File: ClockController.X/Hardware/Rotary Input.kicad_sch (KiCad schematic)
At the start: 7 parts

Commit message: Updated most footprints
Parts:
- C7, C8, C9: footprint Clock Controller:CAP_0603 -> Capacitor_SMD:C_0603_1608Metric
- R12, R13, R8: footprint Clock Controller:RES_0603 -> Resistor_SMD:R_0603_1608Metric
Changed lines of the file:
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@@
 			)
 		)
-		(property "Footprint" "Clock Controller:CAP_0603"
+		(property "Footprint" "Capacitor_SMD:C_0603_1608Metric"
 			(at 111.76 82.55 0)
 			(effects
@@
 			)
 		)
-		(property "Footprint" "Clock Controller:CAP_0603"
+		(property "Footprint" "Capacitor_SMD:C_0603_1608Metric"
 			(at 111.76 132.08 0)
 			(effects
@@
 			)
 		)
-		(property "Footprint" "Clock Controller:RES_0603"
+		(property "Footprint" "Resistor_SMD:R_0603_1608Metric"
 			(at 123.19 82.55 0)
 			(effects
@@
 			)
 		)
-		(property "Footprint" "Clock Controller:CAP_0603"
+		(property "Footprint" "Capacitor_SMD:C_0603_1608Metric"
 			(at 182.88 132.08 0)
 			(effects
@@
 			)
 		)
-		(property "Footprint" "Clock Controller:RES_0603"
+		(property "Footprint" "Resistor_SMD:R_0603_1608Metric"
 			(at 123.19 113.03 0)
 			(effects
@@
 			)
 		)
-		(property "Footprint" "Clock Controller:RES_0603"
+		(property "Footprint" "Resistor_SMD:R_0603_1608Metric"
 			(at 173.99 113.03 0)
 			(effects

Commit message: Replacing many thin traces with poured zones.
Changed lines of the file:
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@@
 (kicad_sch
-	(version 20231120)
+	(version 20250114)
 	(generator "eeschema")
-	(generator_version "8.0")
+	(generator_version "9.0")
 	(paper "A4")
+	(text "10k"
+		(exclude_from_sim no)
+		(at 124.46 114.595 90)
+		(effects
+			(font
+				(size 1.48 1.48)
+			)
+			(justify left top)
+		)
+	)
+	(text "C7"
+		(exclude_from_sim no)
+		(at 109.849 133.372 90)
+		(effects
+			(font
+				(size 1.48 1.48)
+			)
+			(justify left bottom)
+		)
+	)
+	(text "10k"
+		(exclude_from_sim no)
+		(at 124.46 84.115 90)
+		(effects
+			(font
+				(size 1.48 1.48)
+			)
+			(justify left top)
+		)
+	)
+	(text "C8"
+		(exclude_from_sim no)
+		(at 109.849 83.842 90)
+		(effects
+			(font
+				(size 1.48 1.48)
+			)
+			(justify left bottom)
+		)
+	)
+	(text "10nF"
+		(exclude_from_sim no)
+		(at 184.791 134.354 90)
+		(effects
+			(font
+				(size 1.48 1.48)
+			)
+			(justify left top)
+		)
+	)
+	(text "10k"
+		(exclude_from_sim no)
+		(at 175.26 114.595 90)
+		(effects
+			(font
+				(size 1.48 1.48)
+			)
+			(justify left top)
+		)
+	)
+	(text "R12"
+		(exclude_from_sim no)
+		(at 121.92 114.704 90)
+		(effects
+			(font
+				(size 1.48 1.48)
+			)
+			(justify left bottom)
+		)
+	)
+	(text "C9"
+		(exclude_from_sim no)
+		(at 180.969 133.336 90)
+		(effects
+			(font
+				(size 1.48 1.48)
+			)
+			(justify left bottom)
+		)
+	)
+	(text "10nF"
+		(exclude_from_sim no)
+		(at 113.671 84.824 90)
+		(effects
+			(font
+				(size 1.48 1.48)
+			)
+			(justify left top)
+		)
+	)
+	(text "RC5"
+		(exclude_from_sim no)
+		(at 125.222 61.722 0)
+		(effects
+			(font
+				(size 1.48 1.48)
+			)
+			(justify right bottom)
+		)
+	)
+	(text "RC3"
+		(exclude_from_sim no)
+		(at 171.958 136.144 0)
+		(effects
+			(font
+				(size 1.48 1.48)
+			)
+			(justify left bottom)
+		)
+	)
+	(text "R13"
+		(exclude_from_sim no)
+		(at 172.72 114.704 90)
+		(effects
+			(font
+				(size 1.48 1.48)
+			)
+			(justify left bottom)
+		)
+	)
+	(text "10nF"
+		(exclude_from_sim no)
+		(at 113.671 134.354 90)
+		(effects
+			(font
+				(size 1.48 1.48)
+			)
+			(justify left top)
+		)
+	)
+	(text "RC4"
+		(exclude_from_sim no)
+		(at 125.476 136.144 0)
+		(effects
+			(font
+				(size 1.48 1.48)
+			)
+			(justify right bottom)
+		)
+	)
+	(text "S1"
+		(exclude_from_sim no)
+		(at 127.341 87.63 0)
+		(effects
+			(font
+				(size 1.48 1.48)
+			)
+			(justify left bottom)
+		)
+	)
+	(text "R8"
+		(exclude_from_sim no)
+		(at 121.92 83.805 90)
+		(effects
+			(font
+				(size 1.48 1.48)
+			)
+			(justify left bottom)
+		)
+	)
 	(junction
 		(at 123.19 72.39)
@@
 		)
 	)
-	(text "10k"
-		(exclude_from_sim no)
-		(at 124.46 114.595 90)
-		(effects
-			(font
-				(size 1.48 1.48)
-			)
-			(justify left top)
-		)
-	)
-	(text "C7"
-		(exclude_from_sim no)
-		(at 109.849 133.372 90)
-		(effects
-			(font
-				(size 1.48 1.48)
-			)
-			(justify left bottom)
-		)
-	)
-	(text "10k"
-		(exclude_from_sim no)
-		(at 124.46 84.115 90)
-		(effects
-			(font
-				(size 1.48 1.48)
-			)
-			(justify left top)
-		)
-	)
-	(text "C8"
-		(exclude_from_sim no)
-		(at 109.849 83.842 90)
-		(effects
-			(font
-				(size 1.48 1.48)
-			)
-			(justify left bottom)
-		)
-	)
-	(text "10nF"
-		(exclude_from_sim no)
-		(at 184.791 134.354 90)
-		(effects
-			(font
-				(size 1.48 1.48)
-			)
-			(justify left top)
-		)
-	)
-	(text "10k"
-		(exclude_from_sim no)
-		(at 175.26 114.595 90)
-		(effects
-			(font
-				(size 1.48 1.48)
-			)
-			(justify left top)
-		)
-	)
-	(text "R12"
-		(exclude_from_sim no)
-		(at 121.92 114.704 90)
-		(effects
-			(font
-				(size 1.48 1.48)
-			)
-			(justify left bottom)
-		)
-	)
-	(text "C9"
-		(exclude_from_sim no)
-		(at 180.969 133.336 90)
-		(effects
-			(font
-				(size 1.48 1.48)
-			)
-			(justify left bottom)
-		)
-	)
-	(text "10nF"
-		(exclude_from_sim no)
-		(at 113.671 84.824 90)
-		(effects
-			(font
-				(size 1.48 1.48)
-			)
-			(justify left top)
-		)
-	)
-	(text "RC5"
-		(exclude_from_sim no)
-		(at 125.222 61.722 0)
-		(effects
-			(font
-				(size 1.48 1.48)
-			)
-			(justify right bottom)
-		)
-	)
-	(text "RC3"
-		(exclude_from_sim no)
-		(at 171.958 136.144 0)
-		(effects
-			(font
-				(size 1.48 1.48)
-			)
-			(justify left bottom)
-		)
-	)
-	(text "R13"
-		(exclude_from_sim no)
-		(at 172.72 114.704 90)
-		(effects
-			(font
-				(size 1.48 1.48)
-			)
-			(justify left bottom)
-		)
-	)
-	(text "10nF"
-		(exclude_from_sim no)
-		(at 113.671 134.354 90)
-		(effects
-			(font
-				(size 1.48 1.48)
-			)
-			(justify left top)
-		)
-	)
-	(text "RC4"
-		(exclude_from_sim no)
-		(at 125.476 136.144 0)
-		(effects
-			(font
-				(size 1.48 1.48)
-			)
-			(justify right bottom)
-		)
-	)
-	(text "S1"
-		(exclude_from_sim no)
-		(at 127.341 87.63 0)
-		(effects
-			(font
-				(size 1.48 1.48)
-			)
-			(justify left bottom)
-		)
-	)
-	(text "R8"
-		(exclude_from_sim no)
-		(at 121.92 83.805 90)
-		(effects
-			(font
-				(size 1.48 1.48)
-			)
-			(justify left bottom)
-		)
-	)

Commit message: Updated some footprints
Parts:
- S1: footprint Clock Controller:IC5_PEC11S-929K-S0015_BRN -> Rotary_Encoder_:PEC11S-929K-S0015
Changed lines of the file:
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@@
 			)
 		)
-		(property "Footprint" "Clock Controller:IC5_PEC11S-929K-S0015_BRN"
+		(property "Footprint" "Rotary_Encoder_:PEC11S-929K-S0015"
 			(at 128.27 95.25 0)
 			(effects

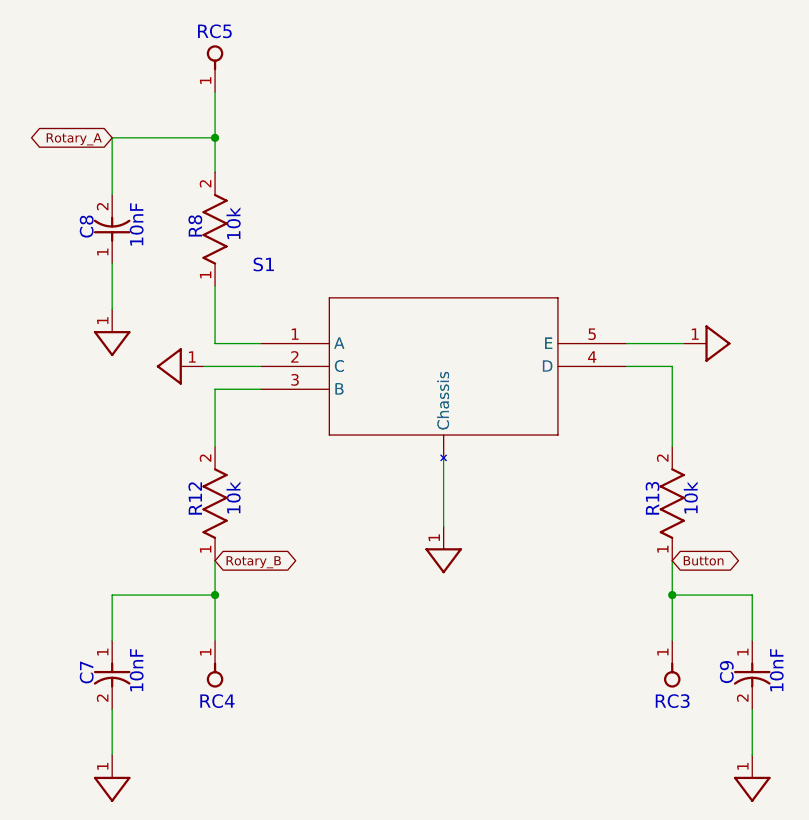
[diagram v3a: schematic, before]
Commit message: Fixed bad pull-up design of I2C cutoff transistors
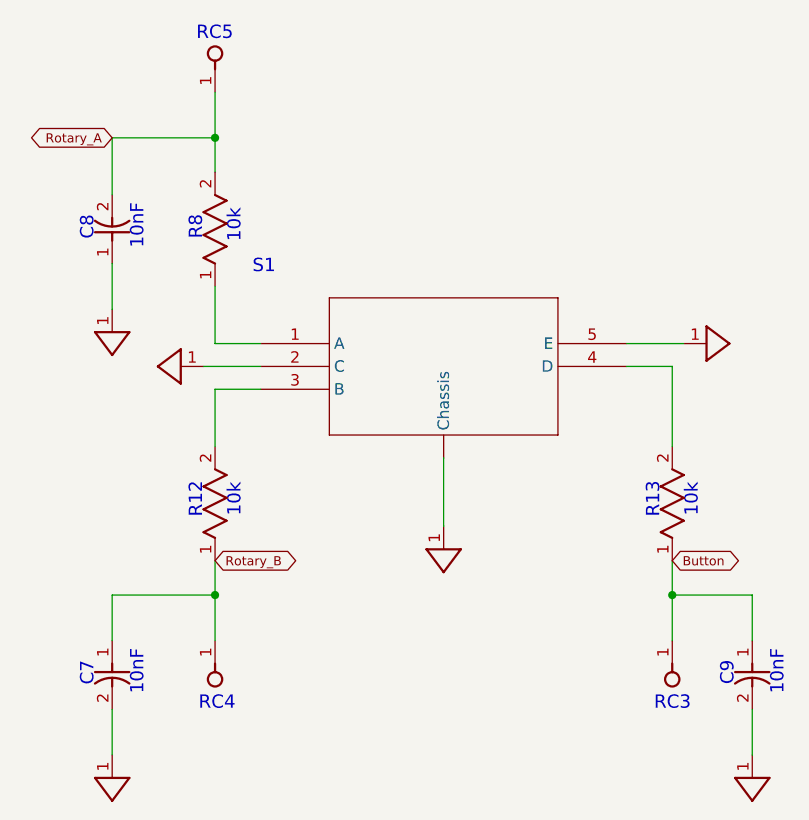
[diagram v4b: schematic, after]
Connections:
- net GND_DIGITAL: no longer S1.6 (Chassis)
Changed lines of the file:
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@@
 		(pin "3"
-		)
-		(pin "6"
 		)
 		(pin "4"
